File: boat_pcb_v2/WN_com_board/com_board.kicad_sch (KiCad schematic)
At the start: 70 parts, among them J1 Conn_01x26_Socket, J16 USB4120-03-C_REVA6, J5 Conn_01x26_Socket, J7 XBP9B-DMUTB002, J8 Conn_01x02_Pin, J9 Conn_01x26_Socket, Q1 NMOS, U1 Particle_B404X, U16 BSS123-7-F, U17 BSS123-7-F, U18 BSS123-7-F, U2 AP62301WU-7, U3 AP62301WU-7

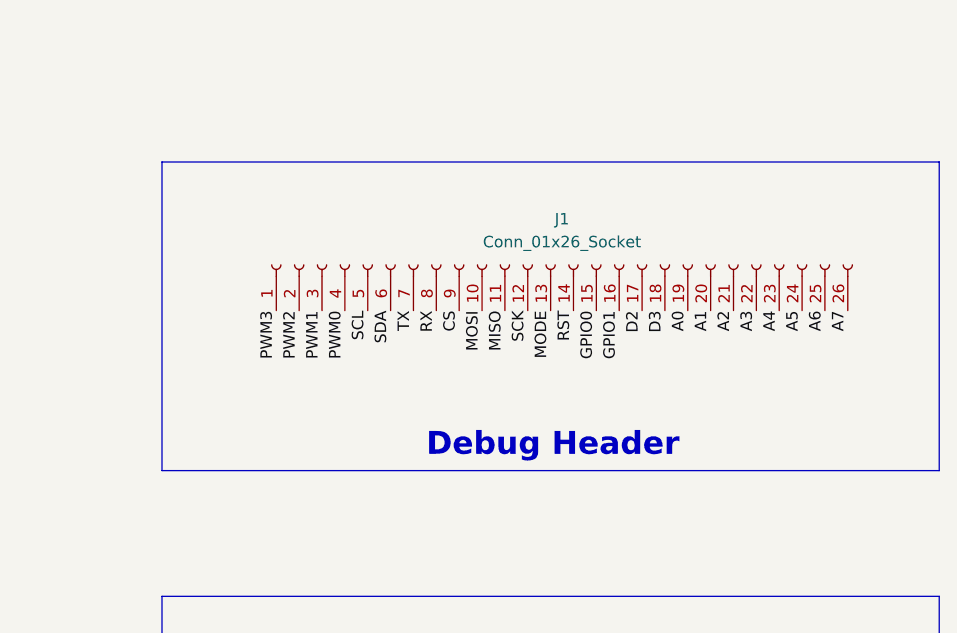
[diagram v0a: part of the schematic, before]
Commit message: minor updates related to board layout
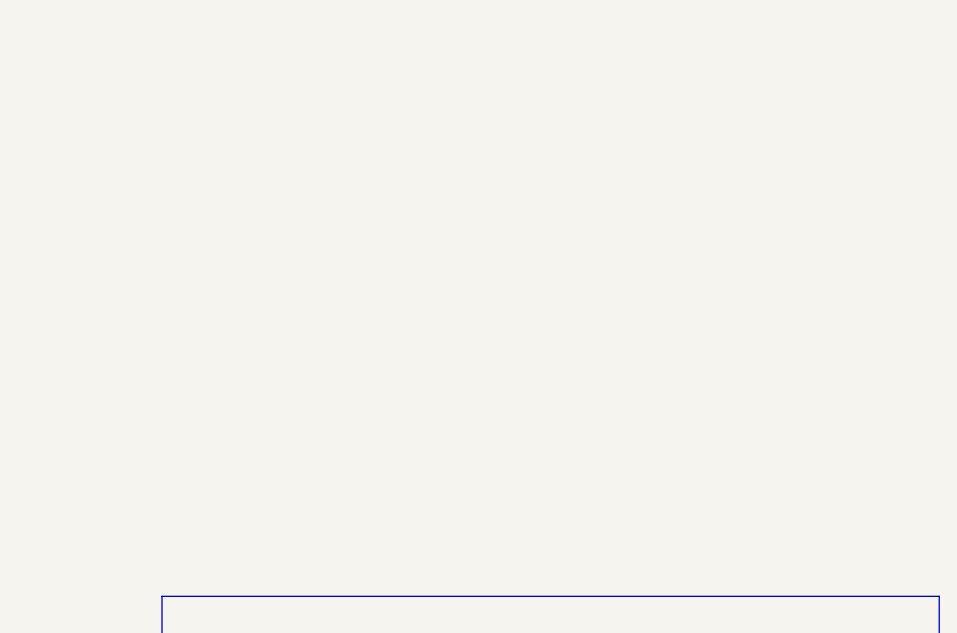
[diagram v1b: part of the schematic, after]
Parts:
- removed J1: Conn_01x26_Socket, Connector_PinHeader_2.54mm:PinHeader_1x26_P2.54mm_Vertical, symbol Connector:Conn_01x26_Socket
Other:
- note removed: "Debug Header"
